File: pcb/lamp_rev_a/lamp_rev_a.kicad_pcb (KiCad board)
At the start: 4 copper layers, 100 x 80 mm, 107 parts, among them J1 TYPE-C 3.1 MT 16P, J2 DC-005-5A-2.0, J3 DB128H-5.08-2P-BK-S, Q1 AO3400A, Q2 MMBT3904, Q3 MMBT3904, Q4 MMBT3904, Q5 MMBT3904, Q6 MMBT3904, Q7 MMBT3904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

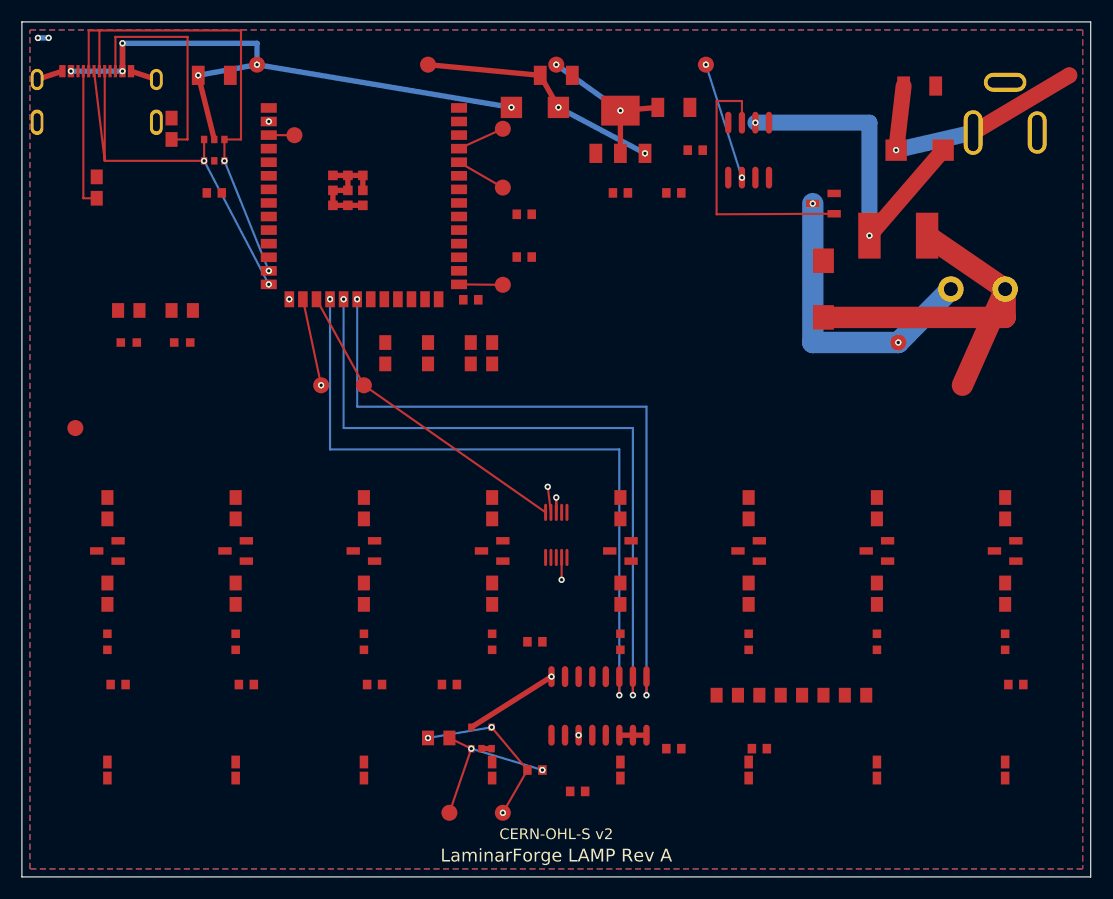
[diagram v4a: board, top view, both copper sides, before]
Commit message: Add LAMP Rev A assembly fixture readability gate
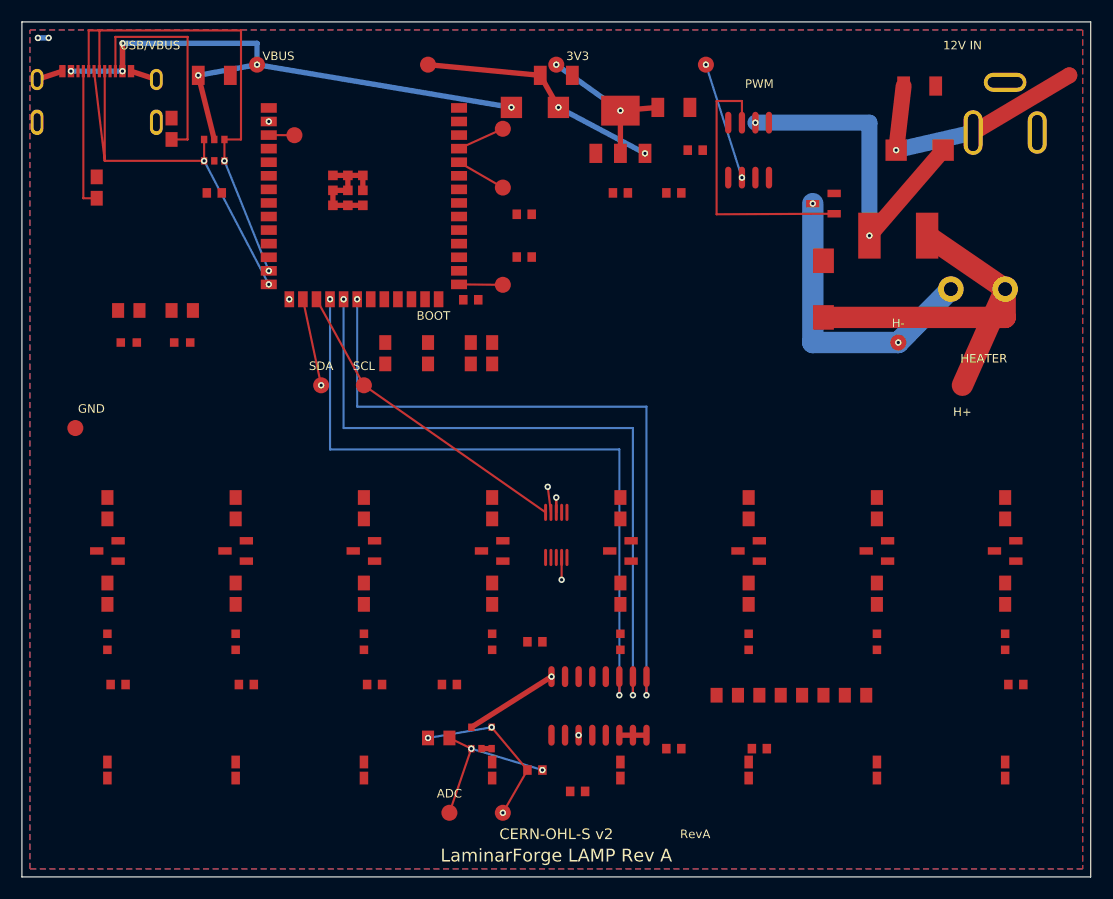
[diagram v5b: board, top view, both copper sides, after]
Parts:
- removed the C21 at (93.0, 62.0)
- removed the Q1 at (75.0, 17.0)
- removed the U2 at (18.0, 12.0)
- added D1: SS34, lcsc:SMA_L4.3-W2.6-LS5.2-RD, F.Cu at (48.0, 8.00)
- added D13: SS34, lcsc:SMA_L4.3-W2.6-LS5.2-RD, F.Cu at (84.0, 12.0)
- added J3: DB128H-5.08-2P-BK-S, lcsc:TERM-BLOCK-5.08-2P, F.Cu at (92.0, 25.0)
- C21: renamed from D13; value SS34 -> 100nF; footprint lcsc:SMA_L4.3-W2.6-LS5.2-RD -> lcsc:C0603
- Q1: renamed from J3; value DB128H-5.08-2P-BK-S -> AO3400A; footprint lcsc:TERM-BLOCK-5.08-2P -> lcsc:SOT-23-3_L2.9-W1.3-P1.90-LS2.4-BR
- U2: renamed from D1; value SS34 -> USBLC6-2SC6; footprint lcsc:SMA_L4.3-W2.6-LS5.2-RD -> lcsc:SOT-23-6
- moved C21 50.8 mm to (93.0, 62.0)
- moved U2 30.3 mm to (18.0, 12.0)
- moved Q1 18.8 mm to (75.0, 17.0), turned to 0 degrees
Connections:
- C21 pad 1: +12V_RAW -> (no net)
- C21 pad 2: +12V -> (no net)
- Q1 pad 1: HEATER_SUPPLY -> GATE_DRV
- Q1 pad 2: HEATER_P -> GND
- U2 pad 1: VBUS -> USB_DP
- U2 pad 2: +5V -> GND
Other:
- board text added: "12V IN"
- board text added: "3V3"
- board text added: "ADC"
- board text added: "BOOT"
- board text added: "GND"
- board text added: "H+"
- board text added: "H-"
- board text added: "HEATER"
- board text added: "PWM"
- board text added: "RevA"
- board text added: "SCL"
- board text added: "SDA"
- board text added: "USB/VBUS"
- board text added: "VBUS"
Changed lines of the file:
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@@
     (effects (font (size 1 1) (thickness 0.1)))
+  )
+  (gr_text "USB/VBUS"
+    (at 12 2.200 0)
+    (layer "F.SilkS")
+    (effects (font (size 0.800 0.800) (thickness 0.1)))
+  )
+  (gr_text "12V IN"
+    (at 88 2.200 0)
+    (layer "F.SilkS")
+    (effects (font (size 0.800 0.800) (thickness 0.1)))
+  )
+  (gr_text "HEATER"
+    (at 90 31.500 0)
+    (layer "F.SilkS")
+    (effects (font (size 0.800 0.800) (thickness 0.1)))
+  )
+  (gr_text "VBUS"
+    (at 24 3.200 0)
+    (layer "F.SilkS")
+    (effects (font (size 0.800 0.800) (thickness 0.1)))
+  )
+  (gr_text "3V3"
+    (at 52 3.200 0)
+    (layer "F.SilkS")
+    (effects (font (size 0.800 0.800) (thickness 0.1)))
+  )
+  (gr_text "H+"
+    (at 88 36.500 0)
+    (layer "F.SilkS")
+    (effects (font (size 0.800 0.800) (thickness 0.1)))
+  )
+  (gr_text "H-"
+    (at 82 28.200 0)
+    (layer "F.SilkS")
+    (effects (font (size 0.800 0.800) (thickness 0.1)))
+  )
+  (gr_text "PWM"
+    (at 69 5.800 0)
+    (layer "F.SilkS")
+    (effects (font (size 0.800 0.800) (thickness 0.1)))
+  )
+  (gr_text "BOOT"
+    (at 38.500 27.500 0)
+    (layer "F.SilkS")
+    (effects (font (size 0.800 0.800) (thickness 0.1)))
+  )
+  (gr_text "ADC"
+    (at 40 72.200 0)
+    (layer "F.SilkS")
+    (effects (font (size 0.800 0.800) (thickness 0.1)))
+  )
+  (gr_text "SDA"
+    (at 28 32.200 0)
+    (layer "F.SilkS")
+    (effects (font (size 0.800 0.800) (thickness 0.1)))
+  )
+  (gr_text "SCL"
+    (at 32 32.200 0)
+    (layer "F.SilkS")
+    (effects (font (size 0.800 0.800) (thickness 0.1)))
+  )
+  (gr_text "GND"
+    (at 6.500 36.200 0)
+    (layer "F.SilkS")
+    (effects (font (size 0.800 0.800) (thickness 0.1)))
+  )
+  (gr_text "RevA"
+    (at 63 76 0)
+    (layer "F.SilkS")
+    (effects (font (size 0.800 0.800) (thickness 0.1)))
   )
   (gr_rect
